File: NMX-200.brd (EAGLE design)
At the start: 67.3 x 63.5 mm, 92 parts, among them IC1 AT90USB1287-AU, J1 PJ-002AH, J3 SJ1-2503A, J4 RJHSE-5385-02, J5 SJ1-2503A, J6 SJ1-2503A, Q1 P-CHANNEL_MOSFET, T1 CMPT2369, T2 CMPT2369, T3 CMPT2369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

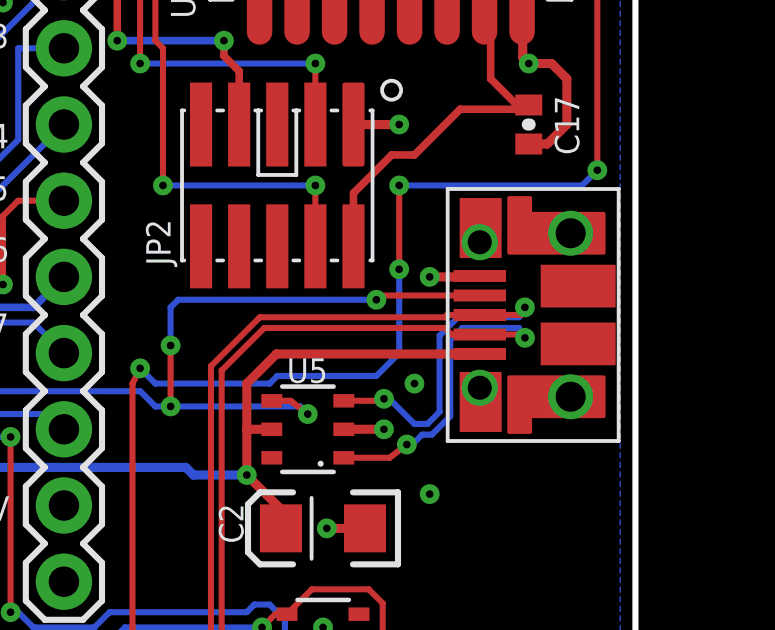
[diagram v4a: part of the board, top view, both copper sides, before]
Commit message: Moved USB connector, fixed DRC errors
Moved the connector slightly closer to the edge of the board and updated
part with revised library part that addresses DRC errors.
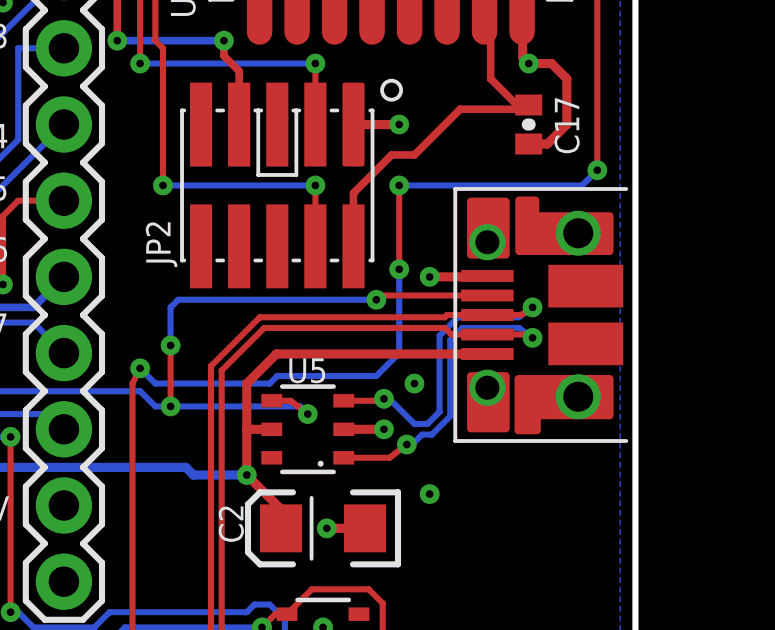
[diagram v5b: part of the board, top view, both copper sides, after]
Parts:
- moved U$5 0.25 mm to (65.4, 34.3)
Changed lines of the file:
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@@
 <attribute name="MPN" value="SMAJ48CA" x="54.61" y="8.89" size="1.778" layer="28" rot="MR0" display="off"/>
 </element>
-<element name="U$5" library="dynamic_perception" package="10118194-0001LF" value="USB_CONN" x="65.151" y="34.29" rot="R90"/>
+<element name="U$5" library="dynamic_perception" package="10118194-0001LF" value="USB_CONN" x="65.405" y="34.29" rot="R90"/>
 </elements>
 <signals>
@@
 <via x="58.928" y="30.48" extent="1-16" drill="0.254"/>
 <via x="60.452" y="35.56" extent="1-16" drill="0.254"/>
-<wire x1="62.121" y1="35.59" x2="62.218" y2="35.56" width="0.3048" layer="1"/>
+<wire x1="62.375" y1="35.59" x2="62.218" y2="35.56" width="0.3048" layer="1"/>
 <wire x1="57.588" y1="30.48" x2="58.928" y2="30.48" width="0.3048" layer="1"/>
 <via x="31.75" y="18.288" extent="1-16" drill="0.8"/>
@@
 <wire x1="55.814" y1="31.43" x2="56.388" y2="30.988" width="0.2032" layer="1"/>
 <wire x1="35.306" y1="45.339" x2="39.37" y2="45.339" width="0.2032" layer="16"/>
-<wire x1="62.121" y1="34.94" x2="58.816" y2="34.94" width="0.2032" layer="1"/>
+<wire x1="62.375" y1="34.94" x2="58.816" y2="34.94" width="0.2032" layer="1"/>
 <wire x1="58.816" y1="34.94" x2="58.674" y2="34.798" width="0.2032" layer="1"/>
 <wire x1="58.674" y1="34.798" x2="52.07" y2="34.798" width="0.2032" layer="16"/>
@@
 <contactref element="R6" pad="1"/>
 <contactref element="U$5" pad="P$2"/>
-<via x="63.627" y="33.528" extent="1-16" drill="0.254"/>
-<wire x1="62.121" y1="33.64" x2="63.642" y2="33.64" width="0.2032" layer="1"/>
-<wire x1="63.642" y1="33.64" x2="63.627" y2="33.528" width="0.2032" layer="1"/>
+<via x="63.881" y="33.528" extent="1-16" drill="0.254"/>
+<wire x1="62.375" y1="33.64" x2="63.642" y2="33.64" width="0.2032" layer="1"/>
+<wire x1="63.642" y1="33.64" x2="63.881" y2="33.528" width="0.2032" layer="1"/>
 <wire x1="57.588" y1="29.53" x2="59.116" y2="29.53" width="0.2032" layer="1"/>
 <wire x1="59.116" y1="29.53" x2="59.69" y2="29.972" width="0.2032" layer="1"/>
@@
 <wire x1="61.1378" y1="33.45435" x2="61.54165" y2="33.8582" width="0.2032" layer="16"/>
 <wire x1="61.54165" y1="33.8582" x2="63.4238" y2="33.8582" width="0.2032" layer="16"/>
-<wire x1="63.4238" y1="33.8582" x2="63.627" y2="33.528" width="0.2032" layer="16"/>
+<wire x1="63.4238" y1="33.8582" x2="63.881" y2="33.528" width="0.2032" layer="16"/>
 <wire x1="33.162" y1="42.418" x2="33.4518" y2="42.418" width="0.2032" layer="1"/>
 <wire x1="33.4518" y1="42.418" x2="34.036" y2="43.0022" width="0.2032" layer="1"/>
@@
 <wire x1="54.93765" y1="33.8582" x2="60.96" y2="33.8582" width="0.2032" layer="1"/>
 <wire x1="60.96" y1="33.8582" x2="61.1782" y2="33.64" width="0.2032" layer="1"/>
-<wire x1="61.1782" y1="33.64" x2="62.121" y2="33.64" width="0.2032" layer="1"/>
+<wire x1="61.1782" y1="33.64" x2="62.375" y2="33.64" width="0.2032" layer="1"/>
 </signal>
 <signal name="D_P">
@@
 <contactref element="R7" pad="1"/>
 <contactref element="U$5" pad="P$3"/>
-<via x="63.627" y="34.544" extent="1-16" drill="0.254"/>
-<wire x1="62.121" y1="34.29" x2="63.5" y2="34.29" width="0.2032" layer="1"/>
-<wire x1="63.5" y1="34.29" x2="63.627" y2="34.544" width="0.2032" layer="1"/>
+<via x="63.881" y="34.544" extent="1-16" drill="0.254"/>
+<wire x1="62.375" y1="34.29" x2="63.5" y2="34.29" width="0.2032" layer="1"/>
+<wire x1="63.5" y1="34.29" x2="63.881" y2="34.544" width="0.2032" layer="1"/>
 <wire x1="57.588" y1="31.43" x2="58.862" y2="31.43" width="0.2032" layer="1"/>
 <wire x1="58.862" y1="31.43" x2="58.928" y2="31.496" width="0.2032" layer="1"/>
@@
 <wire x1="60.7822" y1="33.60165" x2="61.39435" y2="34.2138" width="0.2032" layer="16"/>
 <wire x1="61.39435" y1="34.2138" x2="63.4238" y2="34.2138" width="0.2032" layer="16"/>
-<wire x1="63.4238" y1="34.2138" x2="63.627" y2="34.544" width="0.2032" layer="16"/>
+<wire x1="63.4238" y1="34.2138" x2="63.881" y2="34.544" width="0.2032" layer="16"/>
 <wire x1="33.162" y1="43.688" x2="33.7058" y2="43.688" width="0.2032" layer="1"/>
 <wire x1="33.7058" y1="43.688" x2="34.036" y2="43.3578" width="0.2032" layer="1"/>
@@
 <wire x1="54.79035" y1="34.2138" x2="60.96" y2="34.2138" width="0.2032" layer="1"/>
 <wire x1="60.96" y1="34.2138" x2="61.0362" y2="34.29" width="0.2032" layer="1"/>
-<wire x1="61.0362" y1="34.29" x2="62.121" y2="34.29" width="0.2032" layer="1"/>
+<wire x1="61.0362" y1="34.29" x2="62.375" y2="34.29" width="0.2032" layer="1"/>
 </signal>
 <signal name="PC5">
@@
 <contactref element="D3" pad="A"/>
 <contactref element="U$5" pad="P$1"/>
-<wire x1="62.121" y1="32.99" x2="55.342" y2="32.99" width="0.3048" layer="1"/>
+<wire x1="62.375" y1="32.99" x2="55.342" y2="32.99" width="0.3048" layer="1"/>
 <wire x1="55.342" y1="32.99" x2="54.356" y2="32.004" width="0.3048" layer="1"/>
 <wire x1="54.356" y1="32.004" x2="54.356" y2="30.48" width="0.3048" layer="1"/>
